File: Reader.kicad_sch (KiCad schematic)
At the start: 38 parts, among them J1 Conn_01x04, J2 Amphenol Dubox ‎76383-402LF‎, J3 Conn_01x04, J4 Conn_01x08, J5 Conn_01x10, J6 Conn_01x03, J7 Conn_01x02, Q1 2N7002, Q2 2N7002, Q3 2N7002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

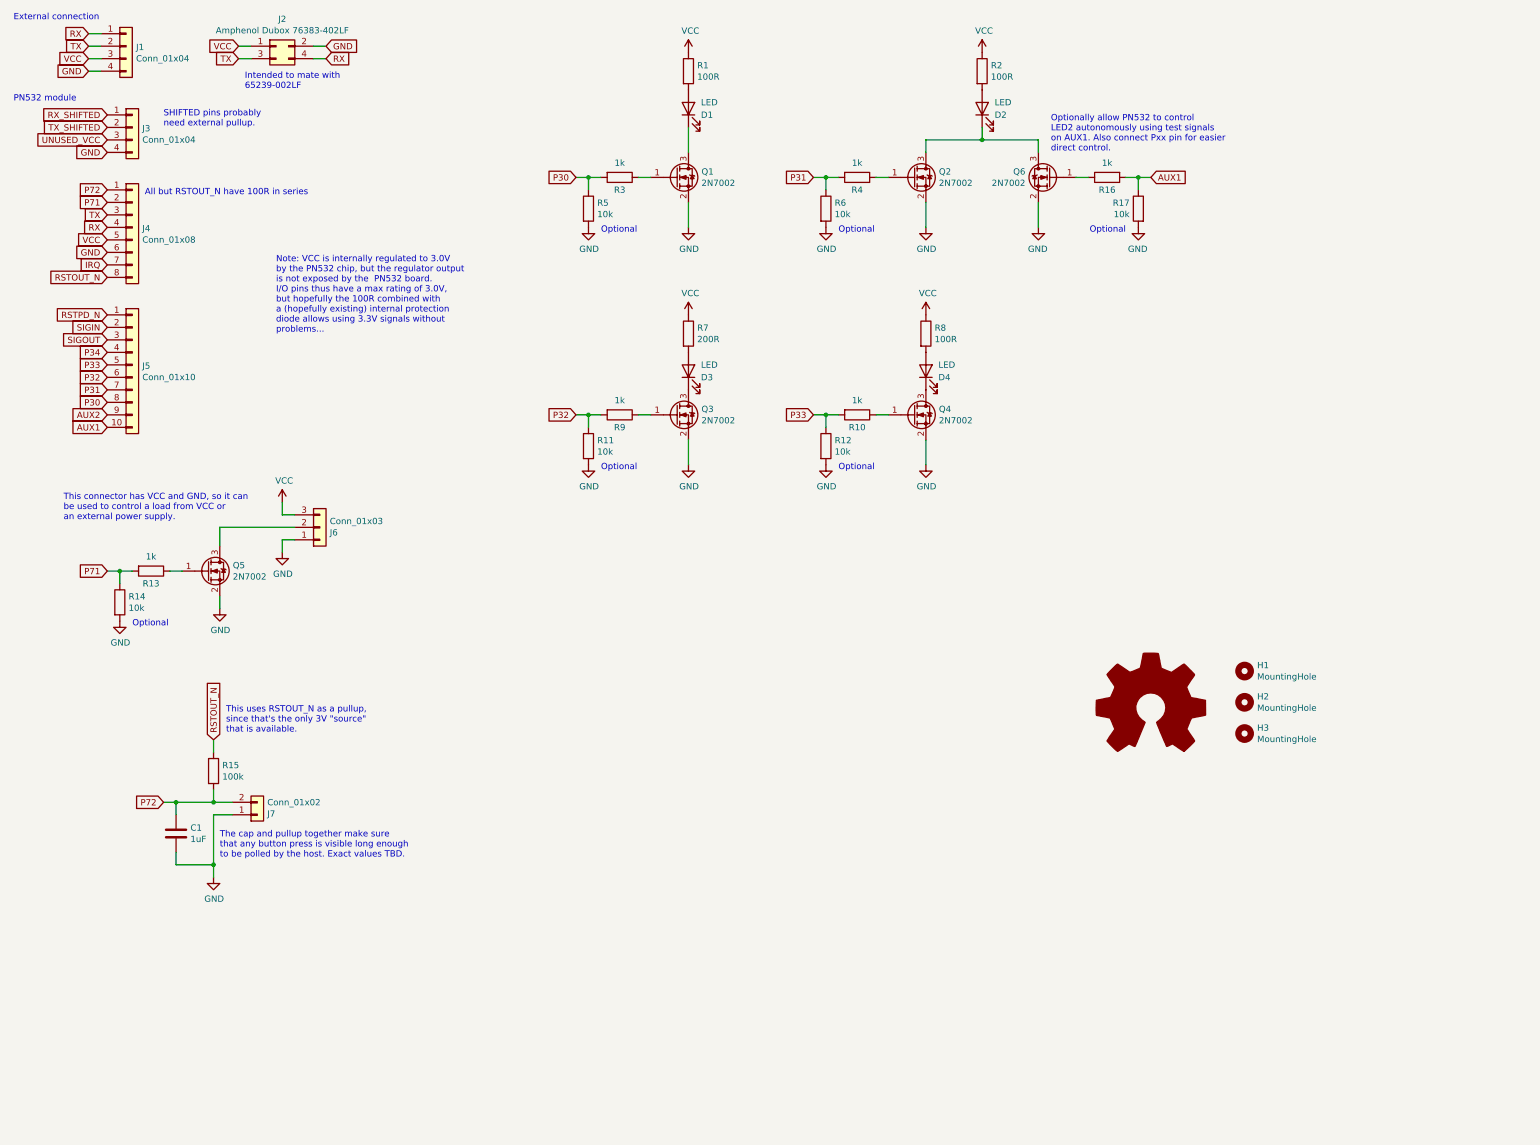
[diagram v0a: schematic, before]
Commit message: Make some schematic changes
This adds some notes, updates some component values to the actually used
values, and maybe some other small changes.
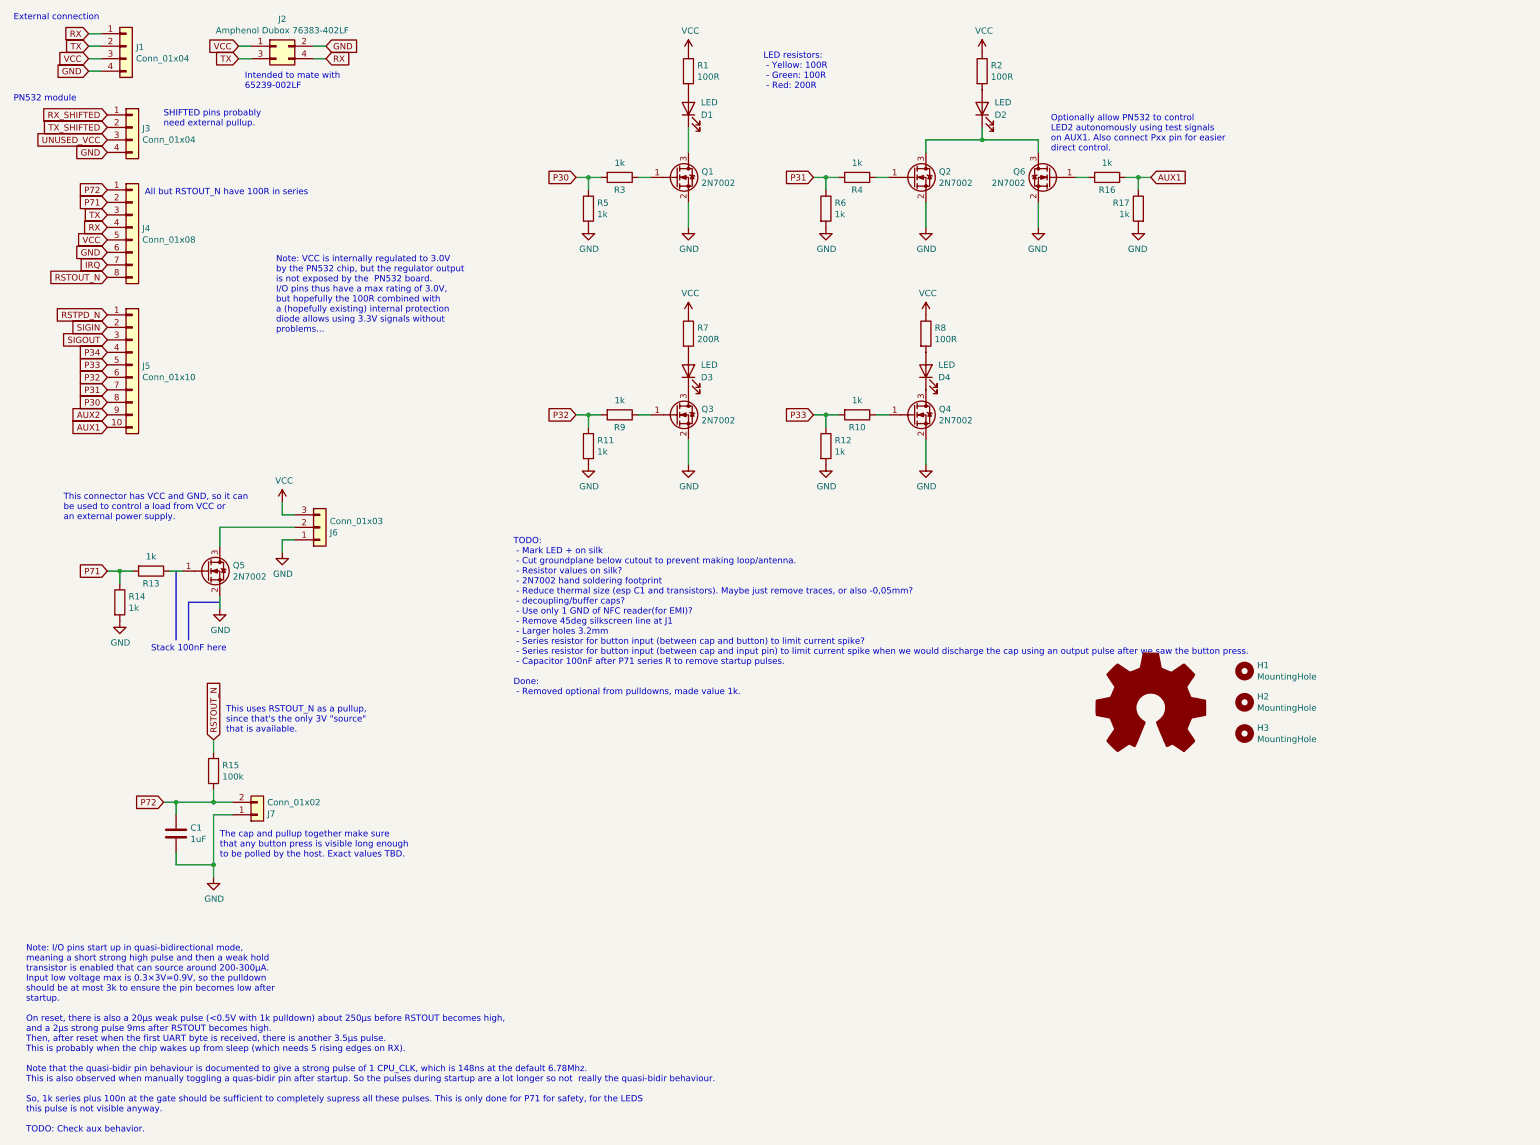
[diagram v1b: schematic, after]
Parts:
- R11, R12, R14, R17, R5, R6: value 10k -> 1k
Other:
- note added: "LED resistors: - Yellow: 100R - Green: 100R - Red: 200R"
- note added: "Note: I/O pins start up in quasi-bidirectional mode, meaning a short strong high pulse and then a weak hold transistor is enabled that can source around 200-300μA. Input low voltage max is 0.3×3V=0.9V, so the pulldown should be at most 3k to ensure the pin becomes low after startup. On reset, there is also a 20μs weak pulse (<0.5V with 1k pulldown) about 250μs before RSTOUT becomes high, and a 2μ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"
- note added: "Stack 100nF here"
- note added: "TODO: - Mark LED + on silk - Cut groundplane below cutout to prevent making loop/antenna. - Resistor values on silk? - 2N7002 hand soldering footprint - Reduce thermal size (esp C1 and transistors). Maybe just remove traces, or also -0,05mm? - decoupling/buffer caps? - Use only 1 GND of NFC reader(for EMI)? - Remove 45deg silkscreen line at J1 - Larger holes 3.2mm - Series resistor for button inp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"
- note removed: "Optional"

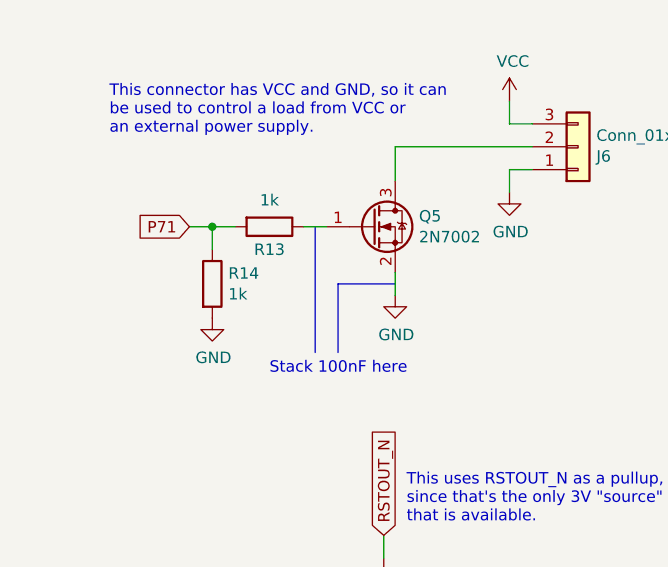
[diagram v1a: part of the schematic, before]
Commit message: Add 100n capacitor on output pin
This takes care of suppressing the startup pulse given by the PN532.
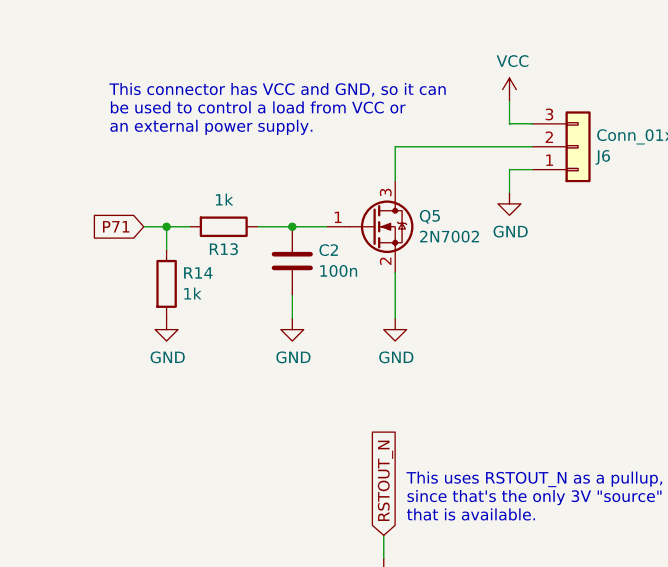
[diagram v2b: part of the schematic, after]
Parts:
- added C2: 100n, Capacitor_SMD:C_0805_2012Metric_Pad1.18x1.45mm_HandSolder, symbol Device:C
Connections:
- net GND: now also C2.2
- net at Q5.1 (G), R13.1: now also C2.1
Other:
- note removed: "Stack 100nF here"
- moved on the sheet: R13, R14
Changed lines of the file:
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@@
   (junction (at 48.26 173.99) (diameter 0) (color 0 0 0 0)
   )
+  (junction (at 45.72 127) (diameter 0) (color 0 0 0 0)
+  )
   (junction (at 55.88 173.99) (diameter 0) (color 0 0 0 0)
   )
-  (junction (at 36.83 127) (diameter 0) (color 0 0 0 0)
+  (junction (at 31.75 127) (diameter 0) (color 0 0 0 0)
   )
   (junction (at 180.34 46.99) (diameter 0) (color 0 0 0 0)
@@
     (stroke (width 0) (type default))
   )
+  (wire (pts (xy 45.72 134.62) (xy 45.72 137.16))
+    (stroke (width 0) (type default))
+  )
   (wire (pts (xy 243.84 49.53) (xy 243.84 46.99))
     (stroke (width 0) (type default))
@@
     (stroke (width 0) (type default))
   )
-  (wire (pts (xy 36.83 127) (xy 39.37 127))
+  (wire (pts (xy 31.75 127) (xy 34.29 127))
     (stroke (width 0) (type default))
   )
@@
     (stroke (width 0) (type default))
   )
+  (wire (pts (xy 45.72 127) (xy 49.53 127))
+    (stroke (width 0) (type default))
+  )
   (wire (pts (xy 129.54 46.99) (xy 132.08 46.99))
     (stroke (width 0) (type default))
@@
     (stroke (width 0) (type default))
   )
-  (wire (pts (xy 46.99 127) (xy 49.53 127))
-    (stroke (width 0) (type default))
-  )
-  (wire (pts (xy 57.15 132.08) (xy 57.15 134.62))
+  (wire (pts (xy 41.91 127) (xy 45.72 127))
+    (stroke (width 0) (type default))
+  )
+  (wire (pts (xy 57.15 132.08) (xy 57.15 137.16))
     (stroke (width 0) (type default))
   )
@@
     (stroke (width 0) (type default))
   )
-  (polyline (pts (xy 48.26 127) (xy 48.26 140.97))
-    (stroke (width 0) (type default))
-  )
   (wire (pts (xy 142.24 46.99) (xy 144.78 46.99))
     (stroke (width 0) (type default))
@@
     (stroke (width 0) (type default))
   )
-  (polyline (pts (xy 50.8 133.35) (xy 50.8 140.97))
-    (stroke (width 0) (type default))
-  )
   (wire (pts (xy 132.08 46.99) (xy 134.62 46.99))
     (stroke (width 0) (type default))
@@
     (stroke (width 0) (type default))
   )
-  (wire (pts (xy 36.83 129.54) (xy 36.83 127))
-    (stroke (width 0) (type default))
-  )
-  (wire (pts (xy 34.29 127) (xy 36.83 127))
-    (stroke (width 0) (type default))
-  )
-  (polyline (pts (xy 57.15 133.35) (xy 50.8 133.35))
+  (wire (pts (xy 31.75 129.54) (xy 31.75 127))
+    (stroke (width 0) (type default))
+  )
+  (wire (pts (xy 29.21 127) (xy 31.75 127))
     (stroke (width 0) (type default))
   )
@@
   (text "This connector has VCC and GND, so it can\nbe used to control a load from VCC or\nan external power supply."
     (at 25.4 116.84 0)
-    (effects (font (size 1.27 1.27)) (justify left bottom))
-  )
-  (text "Stack 100nF here" (at 43.18 143.51 0)
     (effects (font (size 1.27 1.27)) (justify left bottom))
   )
@@
     )
   )
-  (global_label "P71" (shape input) (at 34.29 127 180) (fields_autoplaced)
-    (effects (font (size 1.27 1.27)) (justify right))
-    (property "Intersheetrefs" "${INTERSHEET_REFS}" (at 28.3494 127 0)
+  (global_label "P71" (shape input) (at 29.21 127 180) (fields_autoplaced)
+    (effects (font (size 1.27 1.27)) (justify right))
+    (property "Intersheetrefs" "${INTERSHEET_REFS}" (at 23.2694 127 0)
       (effects (font (size 1.27 1.27)) (justify right) hide)
     )
@@
     )
   )
-  (symbol (lib_id "power:GND") (at 57.15 134.62 0) (unit 1)
-    (in_bom yes) (on_board yes) (dnp no)
-    (property "Reference" "#PWR015" (at 57.15 140.97 0)
-      (effects (font (size 1.27 1.27)) hide)
-    )
-    (property "Value" "GND" (at 57.277 139.0142 0)
-      (effects (font (size 1.27 1.27)))
-    )
-    (property "Footprint" "" (at 57.15 134.62 0)
-      (effects (font (size 1.27 1.27)) hide)
-    )
-    (property "Datasheet" "" (at 57.15 134.62 0)
+  (symbol (lib_id "power:GND") (at 57.15 137.16 0) (unit 1)
+    (in_bom yes) (on_board yes) (dnp no)
+    (property "Reference" "#PWR015" (at 57.15 143.51 0)
+      (effects (font (size 1.27 1.27)) hide)
+    )
+    (property "Value" "GND" (at 57.277 141.5542 0)
+      (effects (font (size 1.27 1.27)))
+    )
+    (property "Footprint" "" (at 57.15 137.16 0)
+      (effects (font (size 1.27 1.27)) hide)
+    )
+    (property "Datasheet" "" (at 57.15 137.16 0)
       (effects (font (size 1.27 1.27)) hide)
     )
@@
     )
   )
-  (symbol (lib_id "Device:R") (at 43.18 127 270) (unit 1)
-    (in_bom yes) (on_board yes) (dnp no)
-    (property "Reference" "R13" (at 43.18 129.54 90)
-      (effects (font (size 1.27 1.27)))
-    )
-    (property "Value" "1k" (at 43.18 124.0536 90)
-      (effects (font (size 1.27 1.27)))
-    )
-    (property "Footprint" "Resistor_SMD:R_0805_2012Metric_Pad1.20x1.40mm_HandSolder" (at 43.18 125.222 90)
-      (effects (font (size 1.27 1.27)) hide)
-    )
-    (property "Datasheet" "~" (at 43.18 127 0)
+  (symbol (lib_id "Device:R") (at 38.1 127 270) (unit 1)
+    (in_bom yes) (on_board yes) (dnp no)
+    (property "Reference" "R13" (at 38.1 129.54 90)
+      (effects (font (size 1.27 1.27)))
+    )
+    (property "Value" "1k" (at 38.1 124.0536 90)
+      (effects (font (size 1.27 1.27)))
+    )
+    (property "Footprint" "Resistor_SMD:R_0805_2012Metric_Pad1.20x1.40mm_HandSolder" (at 38.1 125.222 90)
+      (effects (font (size 1.27 1.27)) hide)
+    )
+    (property "Datasheet" "~" (at 38.1 127 0)
       (effects (font (size 1.27 1.27)) hide)
     )
@@
     )
   )
-  (symbol (lib_id "Device:R") (at 36.83 133.35 0) (unit 1)
-    (in_bom yes) (on_board yes) (dnp no)
-    (property "Reference" "R14" (at 38.608 132.1816 0)
-      (effects (font (size 1.27 1.27)) (justify left))
-    )
-    (property "Value" "1k" (at 38.608 134.493 0)
-      (effects (font (size 1.27 1.27)) (justify left))
-    )
-    (property "Footprint" "Resistor_SMD:R_0805_2012Metric_Pad1.20x1.40mm_HandSolder" (at 35.052 133.35 90)
-      (effects (font (size 1.27 1.27)) hide)
-    )
-    (property "Datasheet" "~" (at 36.83 133.35 0)
+  (symbol (lib_id "Device:R") (at 31.75 133.35 0) (unit 1)
+    (in_bom yes) (on_board yes) (dnp no)
+    (property "Reference" "R14" (at 33.528 132.1816 0)
+      (effects (font (size 1.27 1.27)) (justify left))
+    )
+    (property "Value" "1k" (at 33.528 134.493 0)
+      (effects (font (size 1.27 1.27)) (justify left))
+    )
+    (property "Footprint" "Resistor_SMD:R_0805_2012Metric_Pad1.20x1.40mm_HandSolder" (at 29.972 133.35 90)
+      (effects (font (size 1.27 1.27)) hide)
+    )
+    (property "Datasheet" "~" (at 31.75 133.35 0)
       (effects (font (size 1.27 1.27)) hide)
     )
@@
     )
   )
-  (symbol (lib_id "power:GND") (at 36.83 137.16 0) (unit 1)
-    (in_bom yes) (on_board yes) (dnp no)
-    (property "Reference" "#PWR016" (at 36.83 143.51 0)
-      (effects (font (size 1.27 1.27)) hide)
-    )
-    (property "Value" "GND" (at 36.957 141.5542 0)
-      (effects (font (size 1.27 1.27)))
-    )
-    (property "Footprint" "" (at 36.83 137.16 0)
-      (effects (font (size 1.27 1.27)) hide)
-    )
-    (property "Datasheet" "" (at 36.83 137.16 0)
+  (symbol (lib_id "power:GND") (at 31.75 137.16 0) (unit 1)
+    (in_bom yes) (on_board yes) (dnp no)
+    (property "Reference" "#PWR016" (at 31.75 143.51 0)
+      (effects (font (size 1.27 1.27)) hide)
+    )
+    (property "Value" "GND" (at 31.877 141.5542 0)
+      (effects (font (size 1.27 1.27)))
+    )
+    (property "Footprint" "" (at 31.75 137.16 0)
+      (effects (font (size 1.27 1.27)) hide)
+    )
+    (property "Datasheet" "" (at 31.75 137.16 0)
       (effects (font (size 1.27 1.27)) hide)
     )
@@
         )
       )
+    )
+  )
+  (symbol (lib_id "power:GND") (at 45.72 137.16 0) (unit 1)
+    (in_bom yes) (on_board yes) (dnp no)
+    (property "Reference" "#PWR018" (at 45.72 143.51 0)
+      (effects (font (size 1.27 1.27)) hide)
+    )
+    (property "Value" "GND" (at 45.847 141.5542 0)
+      (effects (font (size 1.27 1.27)))
+    )
+    (property "Footprint" "" (at 45.72 137.16 0)
+      (effects (font (size 1.27 1.27)) hide)
+    )
+    (property "Datasheet" "" (at 45.72 137.16 0)
+      (effects (font (size 1.27 1.27)) hide)
+    )
+    (pin "1")
+    (instances
+      (project "Reader"
+        (path "/f5709391-a389-450b-a647-2f06b3cb0d95"
+          (reference "#PWR018") (unit 1)
+        )
+      )
+    )
+  )
+  (symbol (lib_id "Device:C") (at 45.72 130.81 0) (unit 1)
+    (in_bom yes) (on_board yes) (dnp no)
+    (property "Reference" "C2" (at 48.641 129.6416 0)
+      (effects (font (size 1.27 1.27)) (justify left))
+    )
+    (property "Value" "100n" (at 48.641 131.953 0)
+      (effects (font (size 1.27 1.27)) (justify left))
+    )
+    (property "Footprint" "Capacitor_SMD:C_0805_2012Metric_Pad1.18x1.45mm_HandSolder" (at 46.6852 134.62 0)
+      (effects (font (size 1.27 1.27)) hide)
+    )
+    (property "Datasheet" "~" (at 45.72 130.81 0)
+      (effects (font (size 1.27 1.27)) hide)
+    )
+    (pin "1")
+    (pin "2")
+    (instances
+      (project "Reader"
+        (path "/f5709391-a389-450b-a647-2f06b3cb0d95"
+          (reference "C2") (unit 1)
+        )
+      )
